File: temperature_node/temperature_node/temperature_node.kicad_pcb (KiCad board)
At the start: 2 copper layers, 21 x 34 mm, 29 parts, among them CN1 UART, J1 USB_C_Receptacle_USB2.0_16P, J2 S2B-PH-K-S, U1 SHT40-AD1B-R3, U2 MCP73831-2-OT, U3 MIC5504-3.3YM5, U4 ESP32-C3-WROOM-02

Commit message: Preliminar placement
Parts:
- added TP1: VBUS, TestPoint:TestPoint_Pad_D1.0mm, B.Cu at (131.0, 103.5)
- added TP2: +BATT, TestPoint:TestPoint_Pad_D1.0mm, B.Cu at (141.5, 105.0)
- added TP3: 3V3, TestPoint:TestPoint_Pad_D1.0mm, B.Cu at (133.0, 83.0)
- added TP4: SHT_EN, TestPoint:TestPoint_Pad_D1.0mm, B.Cu at (128.5, 90.0)
- added TP5: GND, TestPoint:TestPoint_Pad_D1.0mm, B.Cu at (124.0, 103.0)
- C2, C3, JP1: moved to B.Cu
- moved C2 20.4 mm to (137.5, 104.0)
- moved C3 15.2 mm to (138.5, 110.0), turned to 180 degrees
- moved J2 0.50 mm to (139.5, 112.0)
- turned JP1 to 180 degrees

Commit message: Import JLCPCB DRC
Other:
- copper layers 2 -> 4
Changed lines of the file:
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@@
 	(generator_version "8.0")
 	(general
-		(thickness 1.6)
+		(thickness 1.600198)
 		(legacy_teardrops no)
 	)
 	(paper "A4")
 	(layers
-		(0 "F.Cu" signal)
-		(31 "B.Cu" signal)
-		(32 "B.Adhes" user "B.Adhesive")
-		(33 "F.Adhes" user "F.Adhesive")
+		(0 "F.Cu" signal "Front")
+		(1 "In1.Cu" signal)
+		(2 "In2.Cu" signal)
+		(31 "B.Cu" signal "Back")
 		(34 "B.Paste" user)
 		(35 "F.Paste" user)
@@
 		(38 "B.Mask" user)
 		(39 "F.Mask" user)
-		(40 "Dwgs.User" user "User.Drawings")
-		(41 "Cmts.User" user "User.Comments")
-		(42 "Eco1.User" user "User.Eco1")
-		(43 "Eco2.User" user "User.Eco2")
 		(44 "Edge.Cuts" user)
 		(45 "Margin" user)
 		(46 "B.CrtYd" user "B.Courtyard")
 		(47 "F.CrtYd" user "F.Courtyard")
-		(48 "B.Fab" user)
 		(49 "F.Fab" user)
-		(50 "User.1" user)
-		(51 "User.2" user)
-		(52 "User.3" user)
-		(53 "User.4" user)
-		(54 "User.5" user)
-		(55 "User.6" user)
-		(56 "User.7" user)
-		(57 "User.8" user)
-		(58 "User.9" user)
 	)
 	(setup
+		(stackup
+			(layer "F.SilkS"
+				(type "Top Silk Screen")
+			)
+			(layer "F.Paste"
+				(type "Top Solder Paste")
+			)
+			(layer "F.Mask"
+				(type "Top Solder Mask")
+				(thickness 0.01)
+			)
+			(layer "F.Cu"
+				(type "copper")
+				(thickness 0.035)
+			)
+			(layer "dielectric 1"
+				(type "core")
+				(thickness 0.480066)
+				(material "FR4")
+				(epsilon_r 4.5)
+				(loss_tangent 0.02)
+			)
+			(layer "In1.Cu"
+				(type "copper")
+				(thickness 0.035)
+			)
+			(layer "dielectric 2"
+				(type "prepreg")
+				(thickness 0.480066)
+				(material "FR4")
+				(epsilon_r 4.5)
+				(loss_tangent 0.02)
+			)
+			(layer "In2.Cu"
+				(type "copper")
+				(thickness 0.035)
+			)
+			(layer "dielectric 3"
+				(type "core")
+				(thickness 0.480066)
+				(material "FR4")
+				(epsilon_r 4.5)
+				(loss_tangent 0.02)
+			)
+			(layer "B.Cu"
+				(type "copper")
+				(thickness 0.035)
+			)
+			(layer "B.Mask"
+				(type "Bottom Solder Mask")
+				(thickness 0.01)
+			)
+			(layer "B.Paste"
+				(type "Bottom Solder Paste")
+			)
+			(layer "B.SilkS"
+				(type "Bottom Silk Screen")
+			)
+			(copper_finish "None")
+			(dielectric_constraints no)
+		)
 		(pad_to_mask_clearance 0)
+		(solder_mask_min_width 0.12)
 		(allow_soldermask_bridges_in_footprints no)
 		(pcbplotparams
@@
 		(tags "capacitor")
 		(property "Reference" "C2"
-			(at 0 1 360)
+			(at 0 1 0)
 			(layer "B.SilkS")
 			(effects
@@
 		)
 		(property "Value" "4u7"
-			(at 0 -1 360)
+			(at 0 -1 0)
 			(layer "B.Fab")
 			(effects
@@
 		)
 		(fp_text user "${REFERENCE}"
-			(at 0 0 360)
+			(at 0 0 0)
 			(layer "B.Fab")
 			(effects

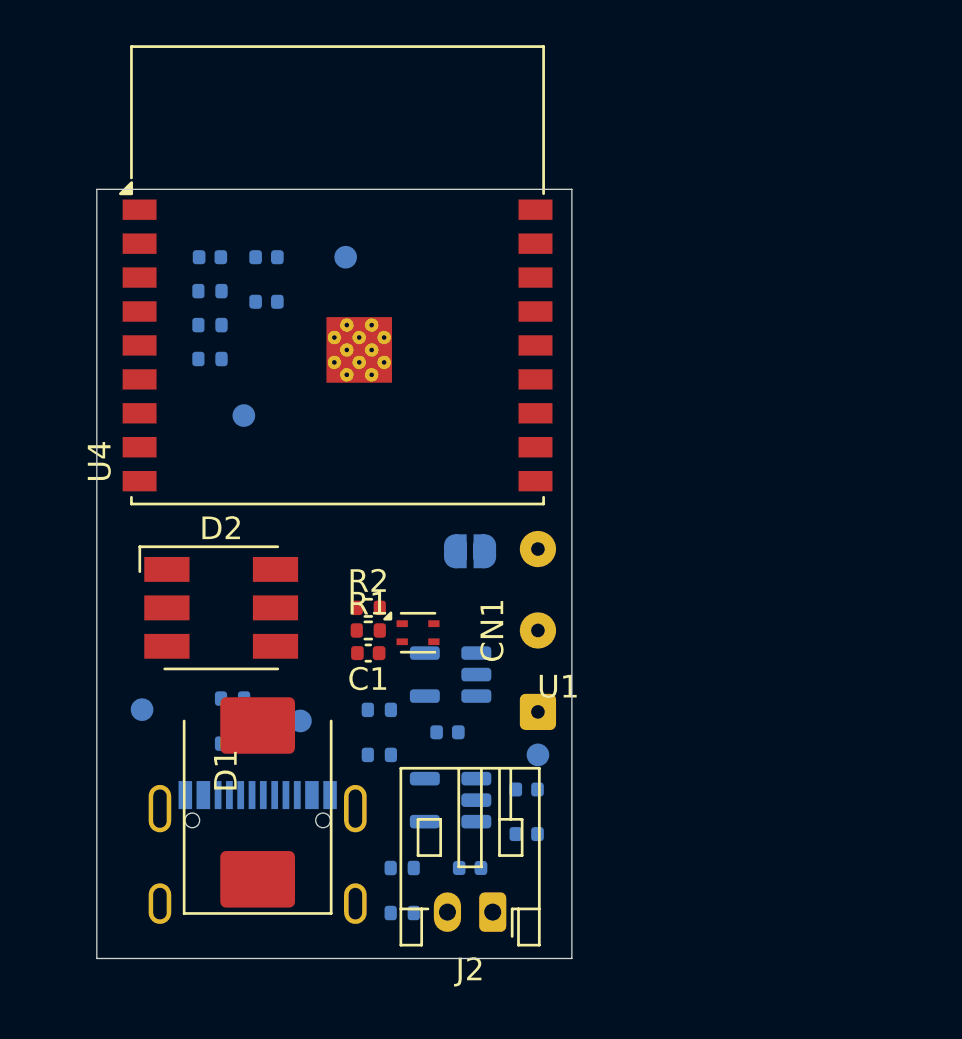
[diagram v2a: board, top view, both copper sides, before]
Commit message: Re-placement to make the PCB smaller
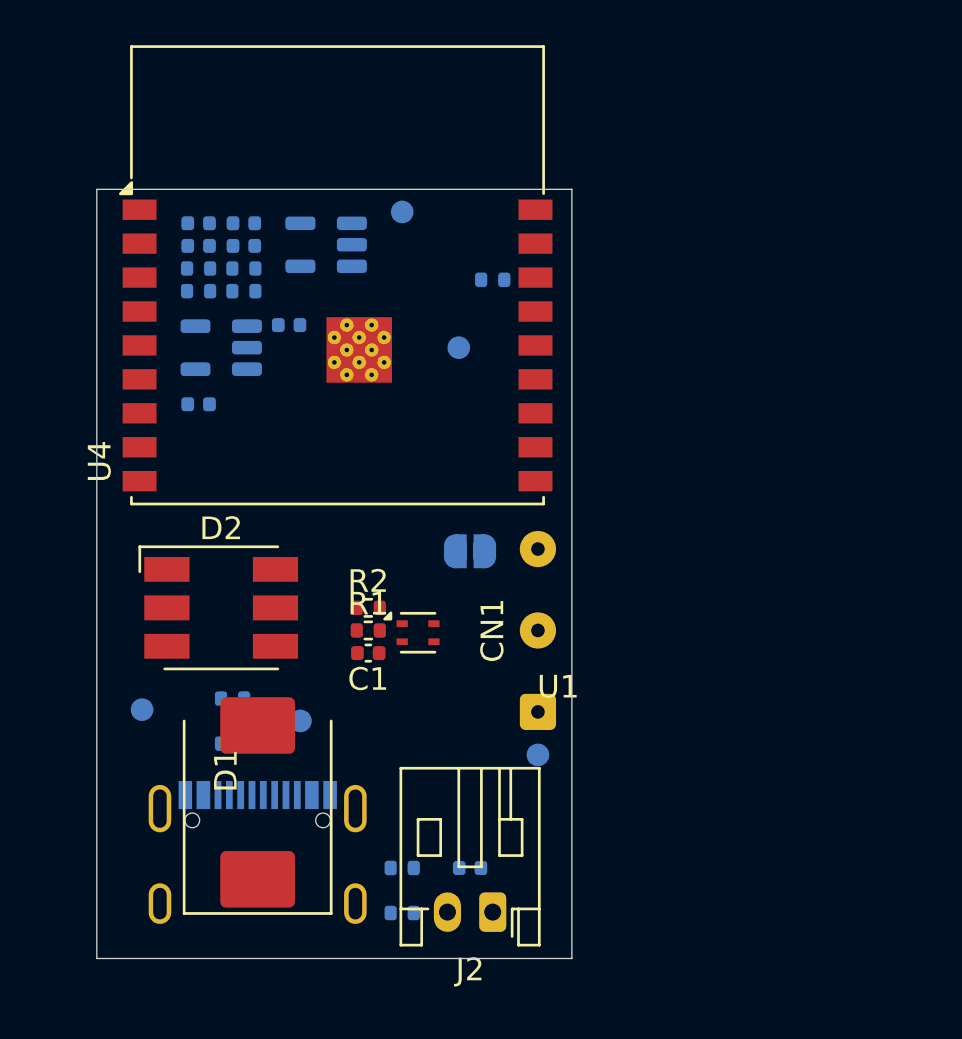
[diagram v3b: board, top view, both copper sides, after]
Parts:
- moved C5 28.8 mm to (128.5, 82.5)
- moved U3 25.2 mm to (132.1, 82.5)
- moved C4 23.1 mm to (130.5, 86.0), turned to 0 degrees
- moved R4 21.4 mm to (128.5, 84.5)
- moved R3 20.2 mm to (126.5, 84.5)
- moved C2 18.2 mm to (126.5, 89.5)
- moved U2 17.7 mm to (127.5, 87.0)
- moved R8 12.5 mm to (139.5, 84.0)
- moved TP4 9.96 mm to (138.0, 87.0)
- moved R9 4.27 mm to (128.5, 83.5)
- moved C8 3.89 mm to (126.5, 82.5), turned to 0 degrees
- moved TP3 3.20 mm to (135.5, 81.0)
- moved R10 2.55 mm to (126.5, 83.5)
- moved C7 1.80 mm to (128.5, 81.5)
- moved C6 1.58 mm to (126.5, 81.5), turned to 0 degrees

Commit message: Continue making the board smaller
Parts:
- D1, D2: moved to B.Cu
- J2: footprint Connector_JST:JST_PH_S2B-PH-K_1x02_P2.00mm_Horizontal -> Connector_JST:JST_PH_S2B-PH-SM4-TB_1x02-1MP_P2.00mm_Horizontal; moved to B.Cu
- moved C3 19.1 mm to (157.5, 108.5)
- moved R11 19.1 mm to (154.5, 108.5)
- moved R12 19.1 mm to (154.5, 110.5)
- moved D1 11.8 mm to (127.0, 95.5), turned to 180 degrees
- moved D2 11.4 mm to (136.5, 91.5), turned to 180 degrees
- moved R5 9.92 mm to (120.5, 96.0)
- moved R6 9.92 mm to (120.5, 98.0)
- moved C1 9.47 mm to (126.5, 106.3)
- moved R1 9.47 mm to (126.5, 105.3)
- moved R2 9.47 mm to (126.5, 104.3)
- moved U1 9.47 mm to (128.7, 105.4)
- moved J2 9.17 mm to (137.5, 103.0)
- moved CN1 7.24 mm to (140.7, 95.9), turned to 180 degrees
- moved J1 6.72 mm to (127.4, 104.0)
- moved JP1 5.53 mm to (133.8, 99.0)

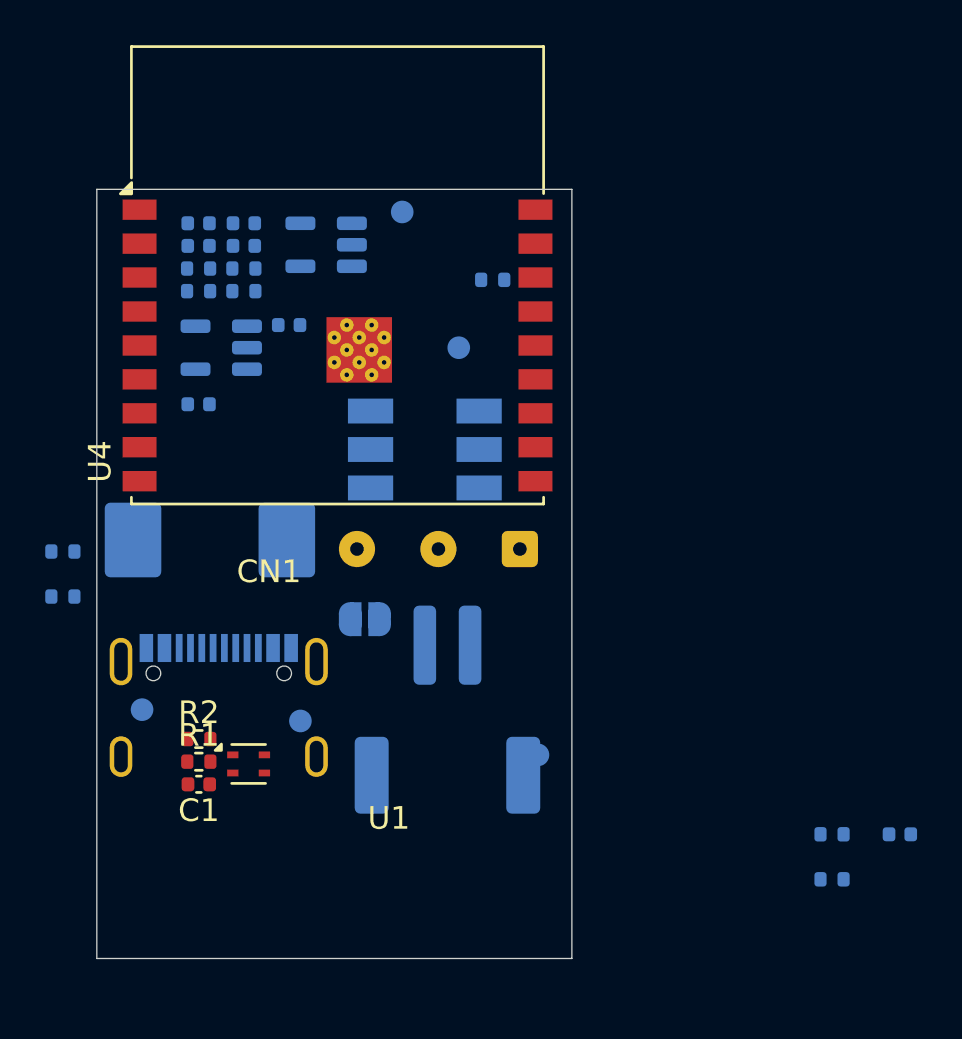
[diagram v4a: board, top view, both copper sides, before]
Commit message: Castellation pins for programming and resize for smaller board
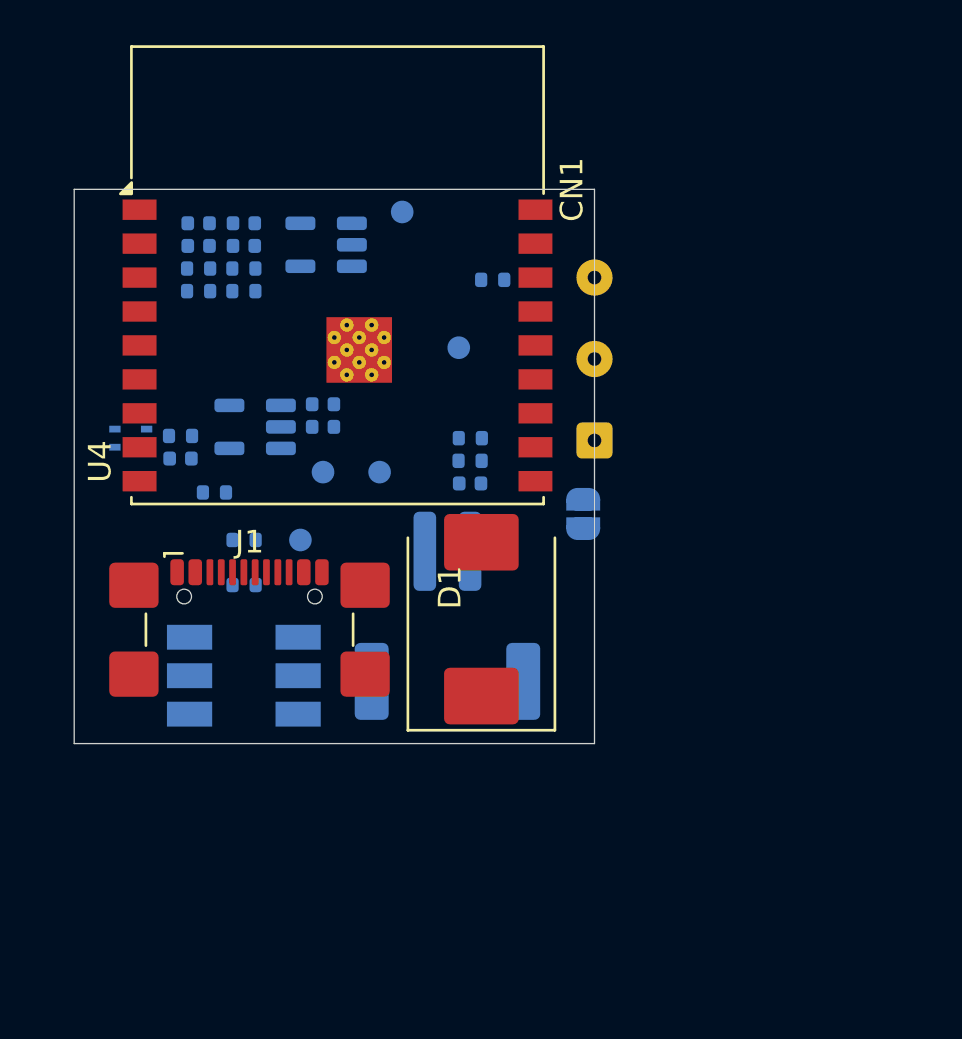
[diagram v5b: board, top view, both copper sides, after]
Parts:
- C1, R1, R2, U1: moved to B.Cu
- D1: moved to F.Cu
- J1: footprint Connector_USB:USB_C_Receptacle_G-Switch_GT-USB-7010ASV -> Connector_USB:USB_C_Receptacle_GCT_USB4110; moved to F.Cu
- moved R12 25.2 mm to (138.5, 91.0), turned to 0 degrees
- moved C3 24.5 mm to (138.5, 93.0), turned to 0 degrees
- moved R11 23.0 mm to (138.5, 92.0), turned to 0 degrees
- moved U1 15.3 mm to (123.5, 91.0), turned to 180 degrees
- moved C1 14.4 mm to (125.7, 91.9), turned to 0 degrees
- moved R1 14.4 mm to (125.7, 90.9), turned to 180 degrees
- moved TP2 14.3 mm to (134.5, 92.5)
- moved TP5 13.2 mm to (132.0, 92.5)
- moved D2 12.8 mm to (128.5, 101.5)
- moved D1 12.5 mm to (139.0, 99.0), turned to 90 degrees
- moved R2 10.9 mm to (127.2, 93.4), turned to 180 degrees
- moved JP1 10.7 mm to (143.5, 94.3), turned to -90 degrees
- moved R5 8.03 mm to (128.5, 95.5)
- moved R6 8.03 mm to (128.5, 97.5)
- moved TP1 8.00 mm to (131.0, 95.5)
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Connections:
- net Net-(CN1-Pin_1) renamed /RX
- net Net-(CN1-Pin_2) renamed /TX
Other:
- board size 21 x 34 mm -> 23 x 24.5 mm

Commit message: Reposition connectors
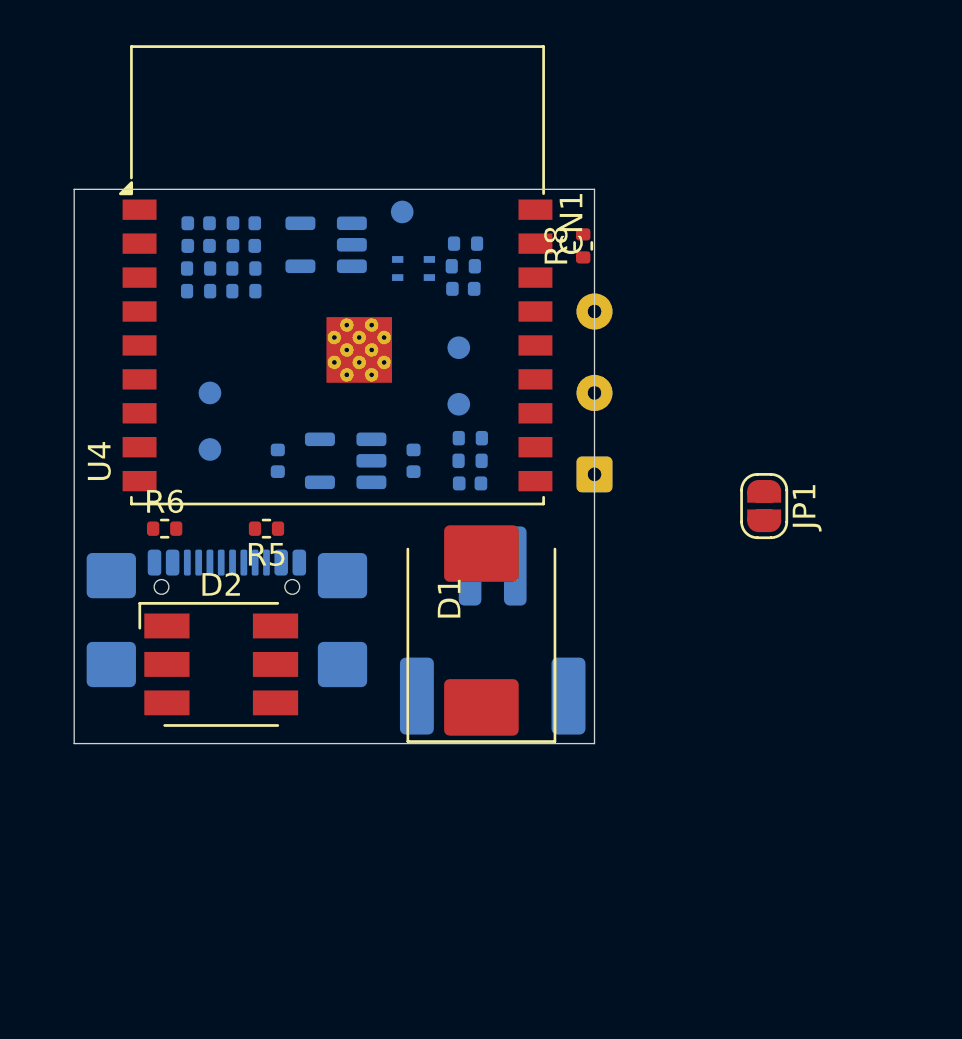
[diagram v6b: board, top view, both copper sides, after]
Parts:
- D2, JP1, R5, R6, R8: moved to F.Cu
- J1: moved to B.Cu
- moved R2 15.6 mm to (138.3, 82.4)
- moved U1 14.6 mm to (136.0, 83.5)
- moved C1 14.6 mm to (138.2, 84.4)
- moved R1 14.6 mm to (138.2, 83.4)
- moved JP1 8.01 mm to (151.5, 94.0)
- moved TP5 6.10 mm to (127.0, 89.0)
- moved TP1 5.66 mm to (127.0, 91.5)
- moved C4 4.72 mm to (136.0, 92.0), turned to 90 degrees
- moved TP2 4.61 mm to (138.0, 89.5)
- moved R6 4.30 mm to (125.0, 95.0), turned to 0 degrees
- moved R8 4.27 mm to (143.5, 82.5), turned to 90 degrees
- moved U2 4.27 mm to (133.0, 92.0)
- moved C2 2.50 mm to (130.0, 92.0), turned to 90 degrees
- moved J2 2.10 mm to (139.5, 99.5)
- moved CN1 1.50 mm to (144.0, 92.6)
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
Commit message: Reposition some componentents and silkscreen
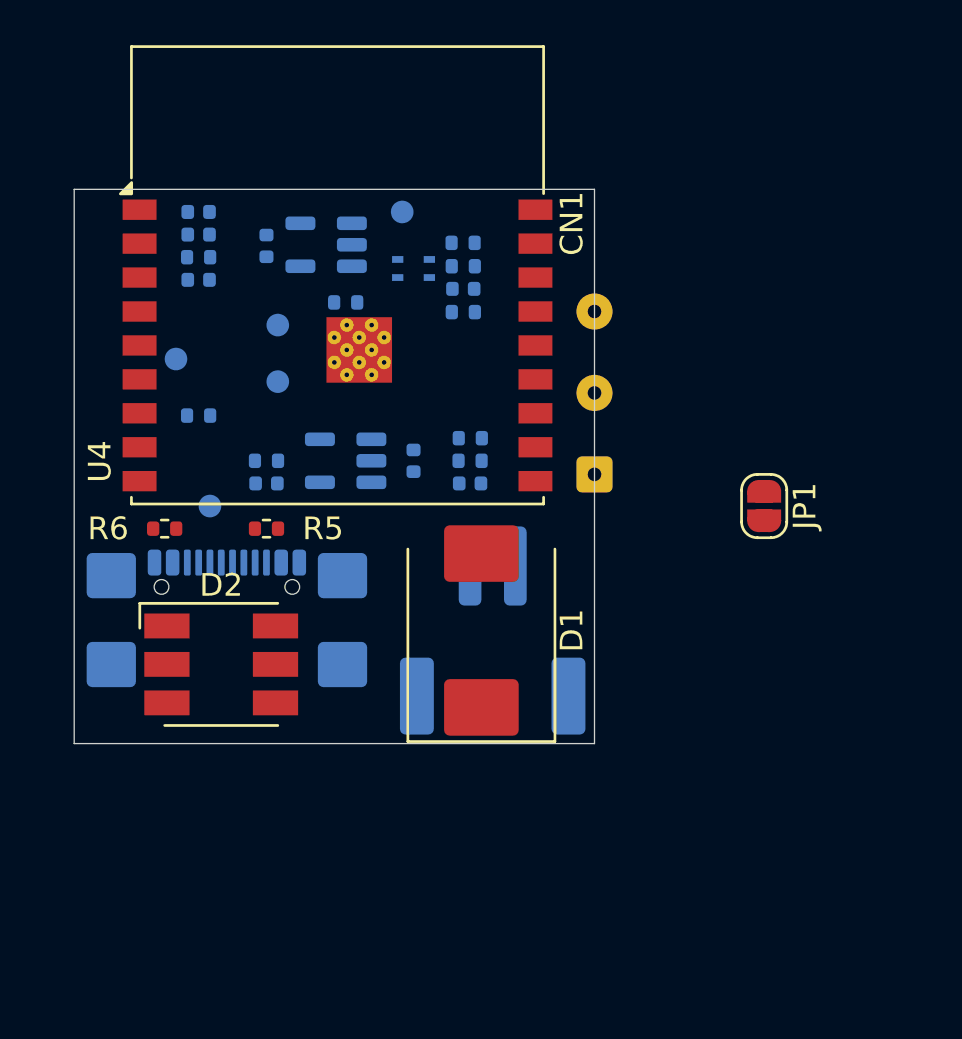
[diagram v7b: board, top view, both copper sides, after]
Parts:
- R8: moved to B.Cu
- moved R3 8.08 mm to (129.5, 92.0)
- moved TP2 8.06 mm to (130.0, 88.5)
- moved TP4 8.06 mm to (130.0, 86.0)
- moved R9 6.80 mm to (126.5, 90.0), turned to 0 degrees
- moved R8 6.05 mm to (138.2, 85.4), turned to 180 degrees
- moved R4 4.53 mm to (133.0, 85.0)
- moved C6 2.50 mm to (126.5, 84.0)
- moved TP1 2.50 mm to (127.0, 94.0)
- moved TP5 2.12 mm to (125.5, 87.5)
- moved C7 2.06 mm to (126.5, 81.0), turned to 0 degrees
- moved C2 1.12 mm to (129.5, 93.0), turned to 180 degrees
- moved C5 1.00 mm to (129.5, 82.5), turned to -90 degrees
- moved C8 0.50 mm to (126.5, 82.0)
- moved R10 0.50 mm to (126.5, 83.0)
- moved R2 0.11 mm to (138.2, 82.4)

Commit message: Placement pre routing
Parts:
- removed D1: 1.5SMC6.8CA, Diode_SMD:D_SMC
- removed D2: APA102, LED_SMD:LED_RGB_5050-6
- added C9: 100n, Capacitor_SMD:C_0402_1005Metric, B.Cu at (127.5, 94.0)
- added D3: WS2812B-2020, LED_SMD:LED_WS2812B-2020_PLCC4_2.0x2.0mm, B.Cu at (132.5, 83.5)
- added U6: USBLC6-2P6, Package_TO_SOT_SMD:SOT-666, B.Cu at (127.5, 96.0)
- J1, J2: moved to F.Cu
- R5, R6: moved to B.Cu
- moved TP5 13.6 mm to (139.0, 89.0)
- moved C5 12.7 mm to (133.4, 94.5)
- moved R4 12.7 mm to (136.9, 97.0)
- moved U3 12.7 mm to (136.0, 94.5)
- moved TP3 10.3 mm to (129.0, 89.0)
- moved C2 9.55 mm to (130.5, 102.5)
- moved C3 9.55 mm to (139.5, 102.5)
- moved C4 9.55 mm to (137.0, 101.5)
- moved R11 9.55 mm to (139.5, 101.5)
- moved R12 9.55 mm to (139.5, 100.5)
- moved R3 9.55 mm to (130.5, 101.5)
- moved U2 9.55 mm to (134.0, 101.5)
- moved TP2 9.49 mm to (139.0, 91.5)
- moved TP4 6.80 mm to (134.0, 91.5)
- moved R6 4.72 mm to (127.5, 99.0)
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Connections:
- J1 pad A6: /D+ -> Net-(J1-D+-PadA6)
- J1 pad A7: /D- -> Net-(J1-D--PadA7)
- J1 pad B6: /D+ -> Net-(J1-D+-PadA6)
- J1 pad B7: /D- -> Net-(J1-D--PadA7)
- U4 pad 4: /LED_CI -> /GPIO5
